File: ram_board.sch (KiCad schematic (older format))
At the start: 6 parts, among them J1 Conn_02x20_Odd_Even, J2 Conn_02x05_Odd_Even, U1 IS61LV5128AL-10TLI, U2 SST39VF040-70-4C-NHE

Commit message: Wiring up
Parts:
- added C1, C2, C3: 100nF, Capacitor_SMD:C_0603_1608Metric_Pad1.05x0.95mm_HandSolder, symbol Device:C_Small
- added C4: 100uF, Capacitor_SMD:C_1206_3216Metric_Pad1.42x1.75mm_HandSolder, symbol Device:C_Small
- added R2: 10K, Resistor_SMD:R_0603_1608Metric_Pad1.05x0.95mm_HandSolder, symbol Device:R_Small
- D1: footprint LED_SMD:LED_0805_2012Metric_Pad1.15x1.40mm_HandSolder -> LED_SMD:LED_0603_1608Metric_Pad1.05x0.95mm_HandSolder
- R1: footprint Resistor_SMD:R_0805_2012Metric_Pad1.15x1.40mm_HandSolder -> Resistor_SMD:R_0603_1608Metric_Pad1.05x0.95mm_HandSolder
- U1: symbol Memory_RAM:IS61LV5128AL-10TLI -> ram_board-rescue:IS61LV5128AL-10TLI-Memory_RAM
- U2: symbol Memory_Flash:SST39VF040-70-4C-NHE -> ram_board-rescue:SST39VF040-70-4C-NHE-Memory_Flash
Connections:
- net labels added: +3.3V
- wire segments 43 -> 112
- no-connect marks 0 -> 9
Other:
- moved on the sheet: D1, J2, R1

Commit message: more cowbell
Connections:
- net D0: now also J1.27 (Pin_27); no longer J1.22 (Pin_22)
- net D1: now also J1.29 (Pin_29); no longer J1.24 (Pin_24)
- net D2: now also J1.30 (Pin_30); no longer J1.26 (Pin_26)
- net D3: now also J1.31 (Pin_31); no longer J1.28 (Pin_28)
- net D6: now also J1.35 (Pin_35); no longer J1.38 (Pin_38)
- net D7: now also J1.38 (Pin_38); no longer J1.40 (Pin_40)
- net RAM_CE: no longer U2.22 (~CE)
- net RAM_OE: no longer U2.24 (~OE)
- net ROM_CE: now also J1.37 (Pin_37), U2.22 (~CE); no longer J1.27 (Pin_27)
- net ROM_OE: now also J1.40 (Pin_40), U2.24 (~OE); no longer J1.29 (Pin_29)
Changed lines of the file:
@@
 	1935 3175 1690 3175
 Wire Wire Line
-	1935 3275 1690 3275
-Wire Wire Line
-	1935 3375 1690 3375
+	1935 3775 1690 3775
 Wire Wire Line
 	1935 3875 1690 3875
@@
 Text Label 1700 3875 0    50   ~ 0
 GND
-Text Label 1695 3275 0    50   ~ 0
+Text Label 1695 3775 0    50   ~ 0
 ROM_CE
-Text Label 1695 3375 0    50   ~ 0
+Text Label 2680 3875 2    50   ~ 0
 ROM_OE
 $Comp
@@
 	2680 2175 2780 2075
 Entry Wire Line
-	1690 3375 1590 3275
+	2680 3875 2780 3775
 Entry Wire Line
 	1690 3175 1590 3075
@@
 	6450 4990 6205 4990
 Text Label 6215 4890 0    50   ~ 0
-RAM_CE
+ROM_CE
 Text Label 6210 4990 0    50   ~ 0
-RAM_OE
+ROM_OE
 Entry Wire Line
 	6205 4990 6105 4890
@@
 	7505 1725 7160 1725
 Wire Wire Line
-	2435 2975 2680 2975
-Wire Wire Line
-	2435 3075 2680 3075
-Wire Wire Line
-	2435 3175 2680 3175
-Wire Wire Line
-	2435 3275 2680 3275
+	1935 3375 1690 3375
+Wire Wire Line
+	2435 3375 2680 3375
+Wire Wire Line
+	1935 3475 1690 3475
 Wire Wire Line
 	2435 3475 2680 3475
@@
 Wire Wire Line
 	2435 3675 2680 3675
-Text Label 2530 2975 2    50   ~ 0
-D0
-Text Label 2530 3075 2    50   ~ 0
-D1
-Text Label 2530 3175 2    50   ~ 0
+Text Label 2530 3375 2    50   ~ 0
 D2
-Text Label 2530 3275 2    50   ~ 0
+Text Label 1840 3475 0    50   ~ 0
 D3
 Text Label 2585 3475 2    50   ~ 0
@@
 D5
 Entry Wire Line
-	2780 2875 2680 2975
-Entry Wire Line
-	2780 2975 2680 3075
-Entry Wire Line
 	2680 3675 2780 3575
 Entry Wire Line
@@
 	2680 3475 2780 3375
 Entry Wire Line
-	2680 3275 2780 3175
-Entry Wire Line
-	2680 3175 2780 3075
+	1690 3475 1590 3375
+Entry Wire Line
+	2680 3375 2780 3275
 Wire Wire Line
 	1690 2875 1935 2875
 Entry Wire Line
-	1690 3275 1590 3175
+	1690 3775 1590 3675
 Entry Wire Line
 	1690 3875 1590 3775
 NoConn ~ 2435 2875
-NoConn ~ 1935 3775
-NoConn ~ 1935 3475
 Wire Wire Line
 	1935 3575 1690 3575
@@
 Entry Wire Line
 	1690 3575 1590 3475
-NoConn ~ 1935 3675
-NoConn ~ 2435 3375
+Wire Wire Line
+	1935 3675 1690 3675
 Wire Wire Line
 	2435 3775 2680 3775
+Text Label 1840 3675 0    50   ~ 0
+D6
+Text Label 2530 3775 2    50   ~ 0
+D7
+Entry Wire Line
+	2680 3775 2780 3675
+Entry Wire Line
+	1690 3675 1590 3575
+NoConn ~ 2435 2975
+Wire Wire Line
+	1935 3275 1690 3275
+Text Label 1840 3275 0    50   ~ 0
+D0
+Text Label 1840 3375 0    50   ~ 0
+D1
+Entry Wire Line
+	1590 3175 1690 3275
+Entry Wire Line
+	1590 3275 1690 3375
+NoConn ~ 2435 3075
+NoConn ~ 2435 3175
+NoConn ~ 2435 3275
 Wire Wire Line
 	2435 3875 2680 3875
-Text Label 2530 3775 2    50   ~ 0
-D6
-Text Label 2530 3875 2    50   ~ 0
-D7
-Entry Wire Line
-	2680 3875 2780 3775
-Entry Wire Line
-	2680 3775 2780 3675
 Wire Bus Line
 	5580 2625 5580 3460
@@
 	7995 2560 7995 3395
 Wire Bus Line
+	2780 1845 2780 3875
+Wire Bus Line
 	6105 2560 6105 4990
 Wire Bus Line
-	2780 1845 2780 3875
-Wire Bus Line
 	1590 1845 1590 3875

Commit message: finished routing, gerbers
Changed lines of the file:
@@
 	0    -1   -1   0
-$EndComp
-$Comp
-L power:+3.3V #PWR07
-U 1 1 5D29524F
-P 2435 4985
-F 0 "#PWR07" H 2435 4835 50  0001 C CNN
-F 1 "+3.3V" H 2450 5158 50  0000 C CNN
-F 2 "" H 2435 4985 50  0001 C CNN
-F 3 "" H 2435 4985 50  0001 C CNN
-	1    2435 4985
-	0    1    1    0
 $EndComp
 Wire Wire Line
@@
 Wire Wire Line
 	2435 3875 2680 3875
+Wire Wire Line
+	2435 4985 2745 4985
+$Comp
+L power:+3.3V #PWR0101
+U 1 1 5D23EE7A
+P 2920 4985
+F 0 "#PWR0101" H 2920 4835 50  0001 C CNN
+F 1 "+3.3V" H 2935 5158 50  0000 C CNN
+F 2 "" H 2920 4985 50  0001 C CNN
+F 3 "" H 2920 4985 50  0001 C CNN
+	1    2920 4985
+	0    1    1    0
+$EndComp
+$Comp
+L power:PWR_FLAG #FLG0101
+U 1 1 5D245CFE
+P 2745 4985
+F 0 "#FLG0101" H 2745 5060 50  0001 C CNN
+F 1 "PWR_FLAG" H 2745 5158 50  0000 C CNN
+F 2 "" H 2745 4985 50  0001 C CNN
+F 3 "~" H 2745 4985 50  0001 C CNN
+	1    2745 4985
+	1    0    0    -1
+$EndComp
+Connection ~ 2745 4985
+Wire Wire Line
+	2745 4985 2920 4985
+$Comp
+L power:PWR_FLAG #FLG0102
+U 1 1 5D2472AD
+P 2435 5285
+F 0 "#FLG0102" H 2435 5360 50  0001 C CNN
+F 1 "PWR_FLAG" H 2435 5458 50  0000 C CNN
+F 2 "" H 2435 5285 50  0001 C CNN
+F 3 "~" H 2435 5285 50  0001 C CNN
+	1    2435 5285
+	0    1    1    0
+$EndComp
 Wire Bus Line
 	5580 2625 5580 3460
@@
 	1590 1845 1590 3875
 Wire Bus Line
-	3690 2625 3690 5055
+	3690 2625 3690 4950
 $EndSCHEMATC

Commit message: Labeling and status leds
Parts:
- added D2, D3: LED, LED_SMD:LED_0603_1608Metric_Pad1.05x0.95mm_HandSolder, symbol Device:LED
- added R3, R4: 360R, Resistor_SMD:R_0603_1608Metric_Pad1.05x0.95mm_HandSolder, symbol Device:R_Small
- added U3: 74LVC2G34, Package_SO:TSOP-6_1.65x3.05mm_P0.95mm, symbol 74xGxx:74LVC2G34
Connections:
- wire segments 114 -> 119
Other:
- moved on the sheet: C1, C2, C3, C4, D1, R1

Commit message: Final Version
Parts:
- removed D2, D3: LED, LED_SMD:LED_0603_1608Metric_Pad1.05x0.95mm_HandSolder, symbol Device:LED
- removed U3: 74LVC2G34, Package_SO:TSOP-6_1.65x3.05mm_P0.95mm, symbol 74xGxx:74LVC2G34
- added D2: RAM Enabled, LED_SMD:LED_2C_0603_1608Metric_Pad1.05x0.95mm_HandSolder, symbol Device:LED_Dual_ACAC
- added D3: ROM Enabled, LED_SMD:LED_2C_0603_1608Metric_Pad1.05x0.95mm_HandSolder, symbol Device:LED_Dual_ACAC
- added R5, R6: 360R, Resistor_SMD:R_0603_1608Metric_Pad1.05x0.95mm_HandSolder, symbol Device:R_Small
- added U3: 74LVC04ADR, Package_SO:SSOP-14_5.3x6.2mm_P0.65mm, symbol 74xx:74LVC04ADR
- R1: value R_Small -> 360R
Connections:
- wire segments 119 -> 134
- no-connect marks 9 -> 11
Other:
- moved on the sheet: J1, J2, R2, R3, R4, U1, U2

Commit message: added BOM and schema docs
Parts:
- added C5: 100nF, Capacitor_SMD:C_0603_1608Metric_Pad1.05x0.95mm_HandSolder, symbol Device:C_Small
- C1, C2, C3: Description (none) -> Multilayer Ceramic Capacitors MLCC - SMD/SMT .1uF 50V X7R 5%; MPN (none) -> CC0603JRX7R9BB104; Manufacturer (none) -> Yageo
- C4: Description (none) -> Multilayer Ceramic Capacitors MLCC - SMD/SMT 100UF 6.3V 10%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; MPN (none) -> GRM31CR60J107KE39L; Manufacturer (none) -> Murata Electronics
- D2: value RAM Enabled -> LED; Description (none) -> Standard LEDs - SMD Red/YelGrn 620/570nm 16/10mcd 65/67mW 5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; MPN (none) -> SML-D22MUWT86; Manufacturer (none) -> ROHM Semiconductor
- D3: value ROM Enabled -> LED; Description (none) -> Standard LEDs - SMD Red/YelGrn 620/570nm 16/10mcd 65/67mW 5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; MPN (none) -> SML-D22MUWT86; Manufacturer (none) -> ROHM Semiconductor
- R1, R3, R4, R5, R6: Description (none) -> Thick Film Resistors - SMD 360 ohm 1%; MPN (none) -> CR0603-FX-3600ELF; Manufacturer (none) -> Bourns
- R2: Description (none) -> Thick Film Resistors - SMD 10K 1% 1/10W; MPN (none) -> CR0603-FX-1002ELF; Manufacturer (none) -> Bourns
- U1: Description (none) -> SRAM 4Mb 512Kx8 10ns Async SRAM 3.3v; MPN (none) -> IS61LV5128AL-10TLI; Manufacturer (none) -> ISSI
- U2: Description (none) -> NOR Flash 4M (512Kx8) 70ns 2.7-3.6V Commercial; MPN (none) -> SST39VF040-70-4C-NHE; Manufacturer (none) -> Microchip Technology
- U3: value 74LVC04ADR -> 74LVC04A; footprint Package_SO:SSOP-14_5.3x6.2mm_P0.65mm -> Package_SO:TSSOP-14_4.4x5mm_P0.65mm; symbol 74xx:74LVC04ADR -> ram_board-rescue:74LVC04ADR-74xx; Description (none) -> Inverters 3.3V HEX INV; MPN (none) -> 74LVC04APW,112; Manufacturer (none) -> Nexperia
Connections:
- net +3V3: now also C5.1
- net GND: now also C5.2
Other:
- note added: "Note: This version requires an synchronous memory controller provided by\n the user implemented on the main DeltaBrd. Version 2 will use an on-board \nMax V 5M40 CPLD as a memory controller and buffer/inverter for the status LED’s."
- note added: "Power Indication"
- note added: "RAM 512Kx8"
- note added: "ROM (NOR Flash) 512Kx8"
- note added: "Red if RAM or ROM disabled, Green enabled"
- moved on the sheet: C1, C2, C3, C4, D1, D2, D3, J1, J2, R1, R2, R3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

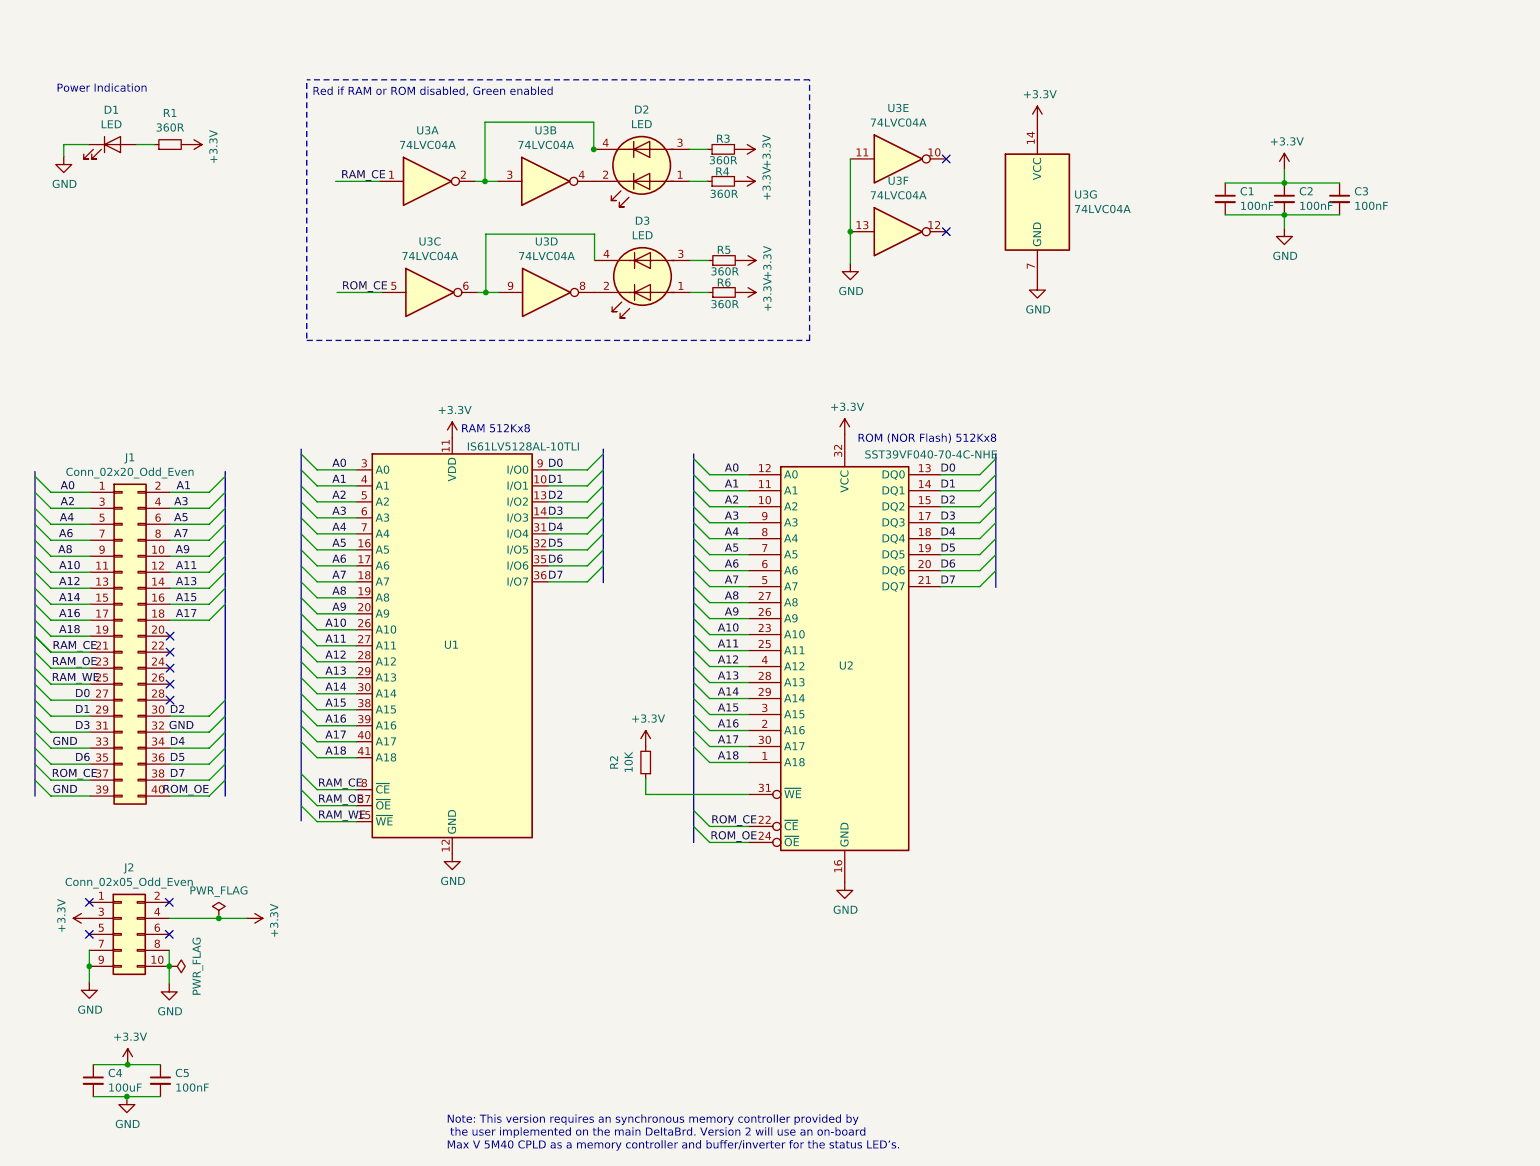
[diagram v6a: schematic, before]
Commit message: fixed leds, spacing
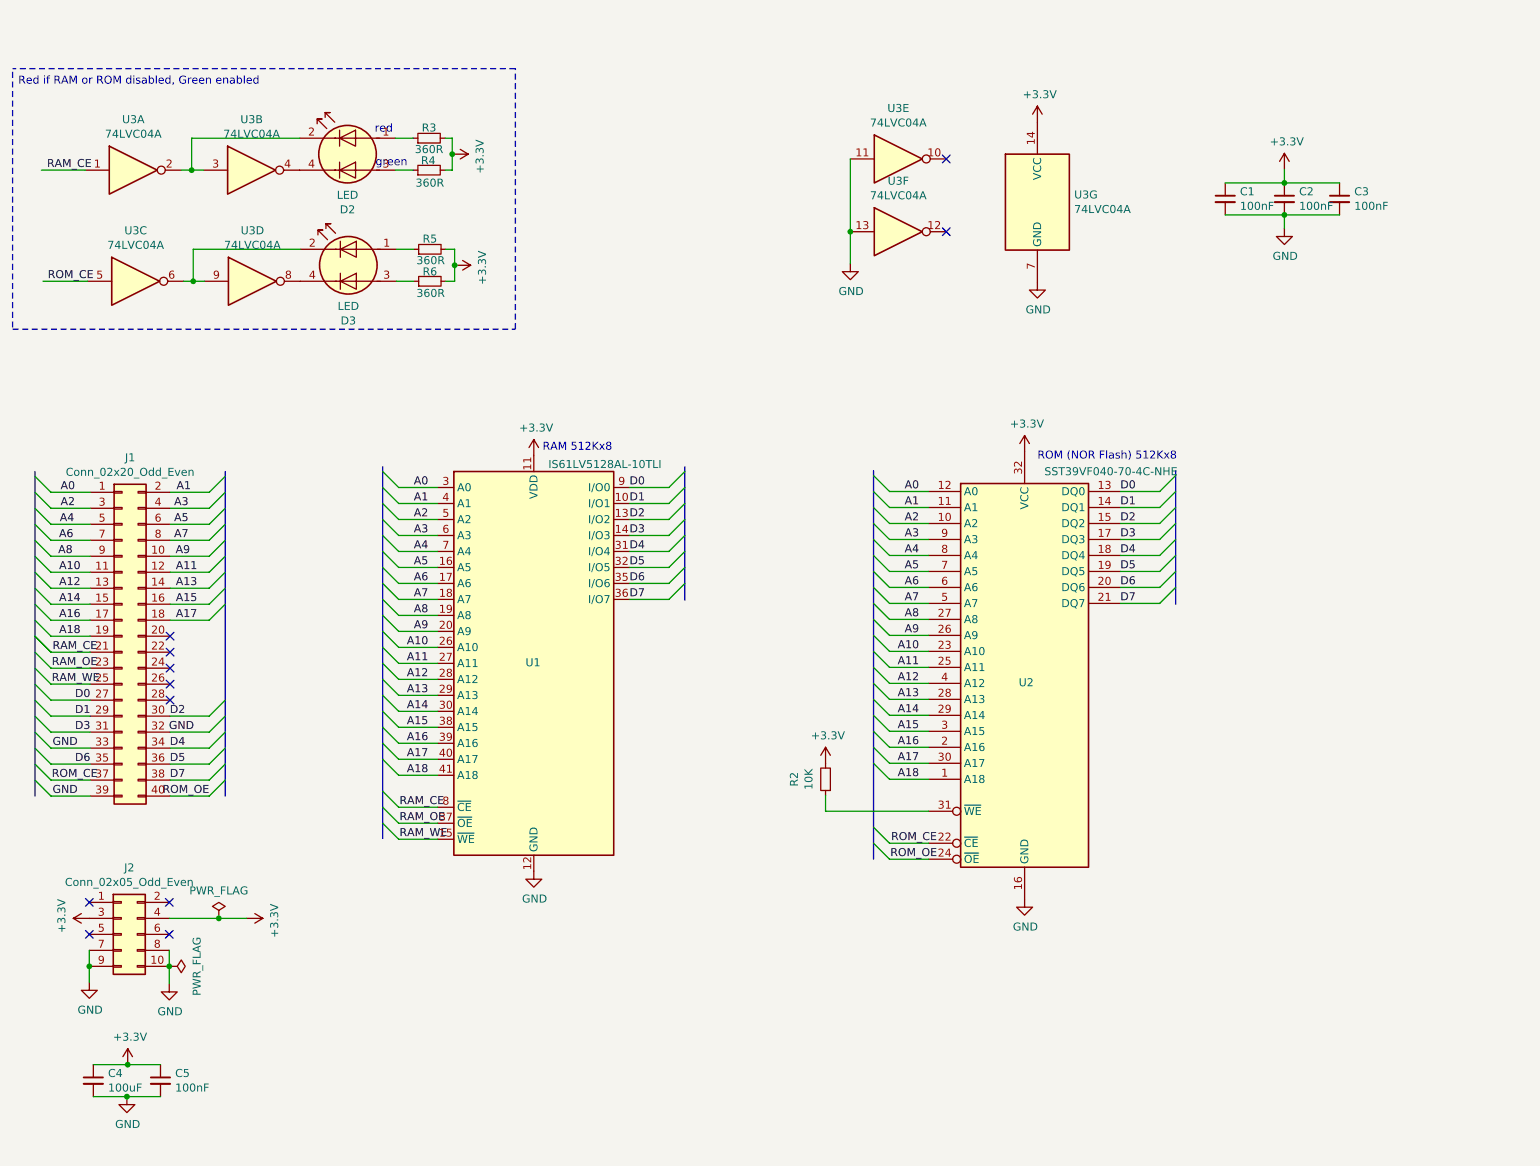
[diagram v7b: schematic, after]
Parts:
- removed D1: LED, LED_SMD:LED_0603_1608Metric_Pad1.05x0.95mm_HandSolder, symbol Device:LED
- removed R1: 360R, Resistor_SMD:R_0603_1608Metric_Pad1.05x0.95mm_HandSolder, symbol Device:R_Small
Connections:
- net at D2.1 (A1): now also R3.1; no longer R4.1
- net at D2.2 (K1): now also U3.2, U3.3; no longer U3.4
- net at D2.3 (A2): now also R4.1; no longer R3.1
- net at U3.6, U3.9: now also D3.2 (K1); no longer D3.4 (K2)
- net at U3.8: now also D3.4 (K2); no longer D3.2 (K1)
- net at R5.1: now also D3.1 (A1); no longer D3.3 (A2)
- net at R6.1: now also D3.3 (A2); no longer D3.1 (A1)
- new net: D2.4 (K2), U3.4
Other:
- note added: "green"
- note added: "red"
- note removed: "Note: This version requires an synchronous memory controller provided by\n the user implemented on the main DeltaBrd. Version 2 will use an on-board \nMax V 5M40 CPLD as a memory controller and buffer/inverter for the status LED’s."
- note removed: "Power Indication"
- moved on the sheet: D2, D3, R2, R3, R4, R5, R6, U1, U2, U3A, U3B, U3C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

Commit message: gnd plane stitching
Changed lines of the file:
@@
 Text Label 1895 4750 2    50   ~ 0
 D2
-Text Label 1205 4850 0    50   ~ 0
+Text Label 1070 4850 0    50   ~ 0
 D3
 Text Label 1950 4850 2    50   ~ 0
@@
 Wire Wire Line
 	1800 5150 2045 5150
-Text Label 1205 5050 0    50   ~ 0
+Text Label 1070 5050 0    50   ~ 0
 D6
 Text Label 1895 5150 2    50   ~ 0
@@
 Wire Wire Line
 	1300 4650 1055 4650
-Text Label 1205 4650 0    50   ~ 0
+Text Label 1070 4650 0    50   ~ 0
 D0
-Text Label 1205 4750 0    50   ~ 0
+Text Label 1070 4750 0    50   ~ 0
 D1
 Entry Wire Line
@@
 	-1   0    0    -1
 $EndComp
-Wire Bus Line
-	5020 3190 5020 4025
-Wire Bus Line
-	8090 3215 8090 4050
-Wire Bus Line
-	2145 3220 2145 5250
-Wire Bus Line
-	6200 3215 6200 5645
-Wire Bus Line
-	955  3220 955  5250
-Wire Bus Line
-	3130 3190 3130 5515
 Text Notes 3080 1110 0    50   ~ 0
 red
 Text Notes 3085 1320 0    50   ~ 0
 green
+Wire Bus Line
+	5020 3190 5020 4025
+Wire Bus Line
+	8090 3215 8090 4050
+Wire Bus Line
+	2145 3220 2145 5250
+Wire Bus Line
+	6200 3215 6200 5645
+Wire Bus Line
+	955  3220 955  5250
+Wire Bus Line
+	3130 3190 3130 5515
 $EndSCHEMATC
